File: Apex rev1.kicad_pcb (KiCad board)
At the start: 2 copper layers, 366.4 x 146.1 mm, 230 parts, among them IC1 24SN, IC2 FE1.1S, J1 OLED, J3 USB_A_SMT_FEMALE, J4 USB_A_SMT_FEMALE, P1 Lily58-cache_CONN_01X04, SW1 SW_PUSH, SW2 Rotary_Encoder_Switch, U1 AT90USB1286-MU, X1 12MHz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

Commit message: add ground plane
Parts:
- removed R7: Ferrite 2A, hub_keyboard:R0805
- P1: value Lily58-cache_CONN_01X04 -> Unified C JST
- moved C11 40.8 mm to (337.3, 77.8), turned to 0 degrees
- moved C18 40.0 mm to (319.4, 86.0)
- moved C14 39.8 mm to (331.8, 77.8), turned to 90 degrees
- moved P1 39.3 mm to (334.6, 64.5)
- moved C13 39.1 mm to (319.7, 72.8)
- moved C15 39.1 mm to (333.4, 81.5)
- moved C16 39.1 mm to (319.7, 74.7)
- moved IC2 39.1 mm to (327.2, 77.0)
- moved R17 39.1 mm to (320.2, 70.9)
- moved R18 39.1 mm to (333.6, 74.9)
- moved R8 39.1 mm to (333.6, 73.4)
- moved R9 39.1 mm to (327.4, 69.6)
- moved X1 39.1 mm to (319.4, 82.1)
- moved C17 39.1 mm to (319.4, 79.0)
- moved C22 39.1 mm to (336.9, 80.1)
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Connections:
- net Net-(IC2-Pad15) renamed /USB Hub/DP-
- net Net-(IC2-Pad16) renamed /USB Hub/DP+
- C12 pad +: Net-(C12-Pad+) -> VCC
- C20 pad +: Net-(C12-Pad+) -> VCC
- D1 pad 4: Net-(C12-Pad+) -> VCC
- D2 pad 4: Net-(C12-Pad+) -> VCC
- J3 pad VBUS: Net-(C12-Pad+) -> VCC
- J4 pad VBUS: Net-(C12-Pad+) -> VCC
- R22 pad 2: Net-(C12-Pad+) -> VCC
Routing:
- net VCC: track 63.8 -> 87.6 mm
- net GND: track 41.3 -> 63.1 mm, vias 0 -> 2
- net /USB Hub/DP+: track 0.00 -> 7.25 mm
- net /USB Hub/DP-: track 0.00 -> 6.06 mm
- net Net-(C18-Pad1): track 17.1 -> 12.3 mm
- net /USB Hub/3V3_HUB: track 34.1 -> 33.1 mm
- added copper zone on B.Cu, net GND
- added copper zone on F.Cu, net GND

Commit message: hub controller placement
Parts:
- moved C4 36.3 mm to (466.6, 127.0)
- moved C5 36.3 mm to (462.0, 128.7)
- moved C6 36.3 mm to (457.3, 119.4)
- moved C3 36.3 mm to (453.8, 119.6)
- moved C8 36.3 mm to (458.4, 113.2)
- moved U1 36.3 mm to (465.3, 118.8)
- moved Y1 36.3 mm to (464.5, 109.4)
- moved C1 36.3 mm to (468.7, 109.5)
- moved C2 36.3 mm to (459.7, 109.5)
- moved R4 36.3 mm to (474.8, 120.1)
- moved C11 21.6 mm to (337.1, 99.4)
- moved C14 21.6 mm to (331.5, 99.4)
- moved C17 21.6 mm to (319.2, 100.6)
- moved C22 21.6 mm to (336.6, 101.7)
- moved C9 21.6 mm to (327.0, 89.0)
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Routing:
- net VCC: track 87.6 -> 117.6 mm
- net GND: track 63.1 -> 89.1 mm, vias 2 -> 4
- net Net-(C21-Pad2): track 0.00 -> 19.6 mm
- net /USB Hub/DP+: track 7.25 -> 25.6 mm
- net /USB Hub/DP-: track 6.06 -> 24.3 mm

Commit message: refine sub hub
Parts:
- P1: value Unified C JST -> Lily58-cache_CONN_01X04
- moved D15 5.02 mm to (296.9, 95.9)
- moved D2 3.24 mm to (156.1, 85.2)
- moved C12 0.93 mm to (61.8, 81.4)
- moved D1 0.41 mm to (65.6, 83.6)
- moved R21 0.08 mm to (157.2, 79.0)
- moved R20 0.08 mm to (155.1, 79.0)
- moved R15 0.06 mm to (66.6, 78.9)
- moved R14 0.06 mm to (64.6, 78.9)
- turned R13 to 270 degrees
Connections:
- net Net-(D1-Pad2) renamed /USB Hub/D1-
- net Net-(D1-Pad3) renamed /USB Hub/D1+
- net Net-(D2-Pad2) renamed /USB Hub/D2-
- net Net-(D2-Pad3) renamed /USB Hub/D2+
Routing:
- net VCC: track 117.6 -> 439.3 mm
- net /USB Hub/D1-: track 0.00 -> 280.4 mm, vias 0 -> 2
- net /USB Hub/D1+: track 0.00 -> 279.2 mm, vias 0 -> 2
- net /USB Hub/D2-: track 0.00 -> 191.5 mm, vias 0 -> 2
- net /USB Hub/D2+: track 0.00 -> 190.2 mm, vias 0 -> 2
- net Net-(C19-Pad2): track 0.00 -> 7.06 mm
- net GND: vias 4 -> 6
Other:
- net class Default: via_dia 0.8 -> 0.6222

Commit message: route keys
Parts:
- moved R4 130.4 mm to (348.2, 151.3), turned to 180 degrees
- moved C1 125.9 mm to (354.3, 161.9), turned to 270 degrees
- moved Y1 118.3 mm to (358.5, 161.9), turned to 0 degrees
- moved U1 112.8 mm to (357.7, 152.5), turned to 180 degrees
- moved C4 111.6 mm to (356.4, 144.3), turned to 0 degrees
- moved C2 109.7 mm to (363.3, 161.9), turned to 90 degrees
- moved R3 104.3 mm to (372.4, 179.3), turned to 270 degrees
- moved C8 104.1 mm to (364.6, 158.2), turned to 270 degrees
- moved C5 102.1 mm to (360.9, 142.7), turned to 180 degrees
- moved SW1 98.7 mm to (378.9, 178.7), turned to 0 degrees
- moved C6 97.1 mm to (365.7, 151.9), turned to 90 degrees
- moved C3 90.6 mm to (369.1, 151.8), turned to 0 degrees
- moved D50 17.1 mm to (314.5, 131.1)
- moved D80 16.5 mm to (59.9, 181.2)
- moved D77 15.6 mm to (267.5, 167.3)
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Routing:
- net ROW0: track 0.00 -> 338.9 mm, vias 0 -> 2
- net ROW5: track 0.00 -> 324.7 mm
- net ROW2: track 0.00 -> 319.3 mm
- net ROW1: track 0.00 -> 318.6 mm
- net ROW4: track 0.00 -> 287.7 mm
- net ROW3: track 0.00 -> 249.3 mm
- net COL15: track 0.00 -> 135.2 mm
- net COL10: track 0.00 -> 134.8 mm
- net COL13: track 0.00 -> 124.7 mm, vias 0 -> 1
- net COL11: track 0.00 -> 124.0 mm
- net VCC: track 439.3 -> 562.7 mm
- net D+: track 0.00 -> 119.9 mm
- net COL2: track 0.00 -> 119.6 mm
- net COL12: track 0.00 -> 118.5 mm
- net D-: track 0.00 -> 118.4 mm
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
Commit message: routed keys
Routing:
- net VCC: track 562.7 -> 606.9 mm
- net SDA: track 2.64 -> 35.9 mm, vias 0 -> 2
- net SCL: track 2.85 -> 35.8 mm, vias 0 -> 2
- net GND: track 94.0 -> 115.5 mm, vias 6 -> 8
- net Net-(D20-Pad2): track 0.00 -> 12.6 mm
- net Net-(D36-Pad2): track 0.00 -> 12.1 mm
- net Net-(D23-Pad2): track 0.00 -> 10.8 mm
- net Net-(D22-Pad2): track 0.00 -> 10.4 mm
- net Net-(D21-Pad2): track 0.00 -> 10.4 mm
- net Net-(D25-Pad2): track 0.00 -> 9.66 mm
- net Net-(D24-Pad2): track 0.00 -> 9.65 mm
- net Net-(D26-Pad2): track 0.00 -> 9.33 mm
- net Net-(D34-Pad2): track 0.00 -> 9.03 mm
- net Net-(D33-Pad2): track 0.00 -> 9.01 mm
- net Net-(D27-Pad2): track 0.00 -> 9.00 mm
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
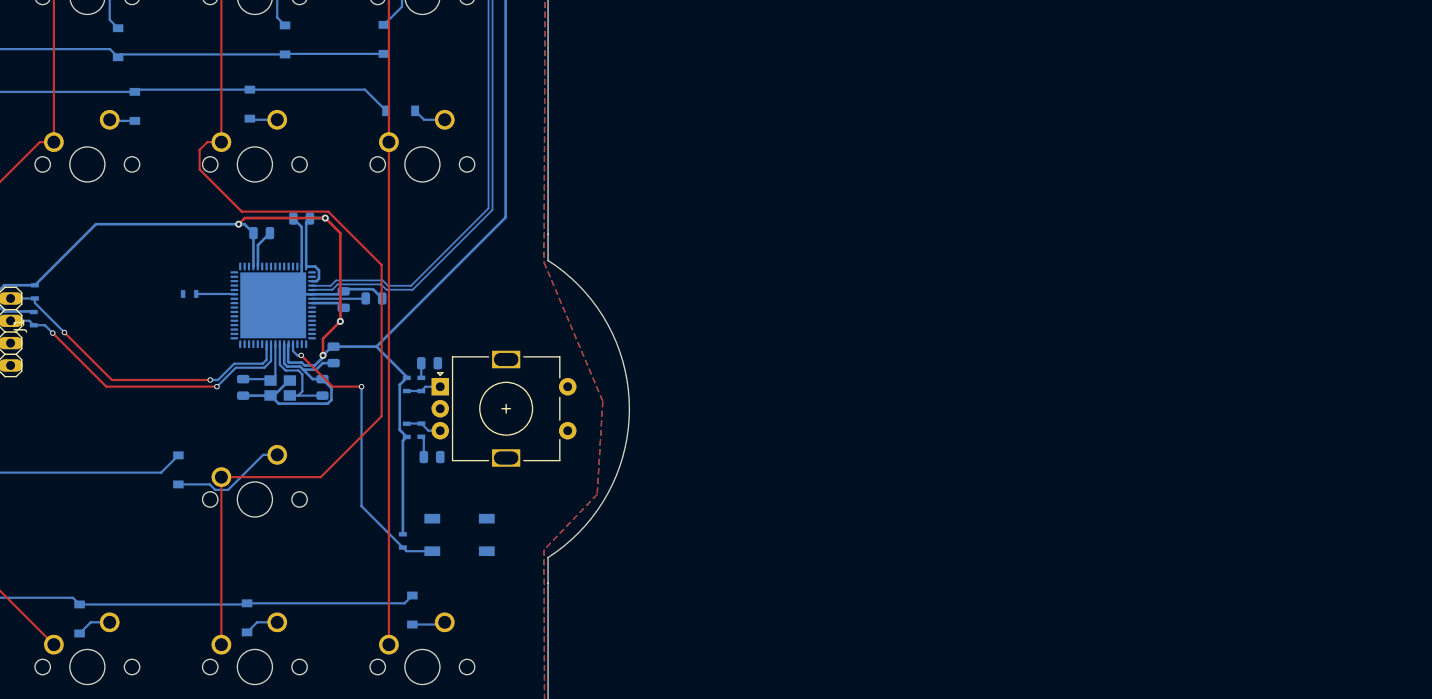
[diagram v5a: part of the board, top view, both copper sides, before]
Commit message: assigned some pins
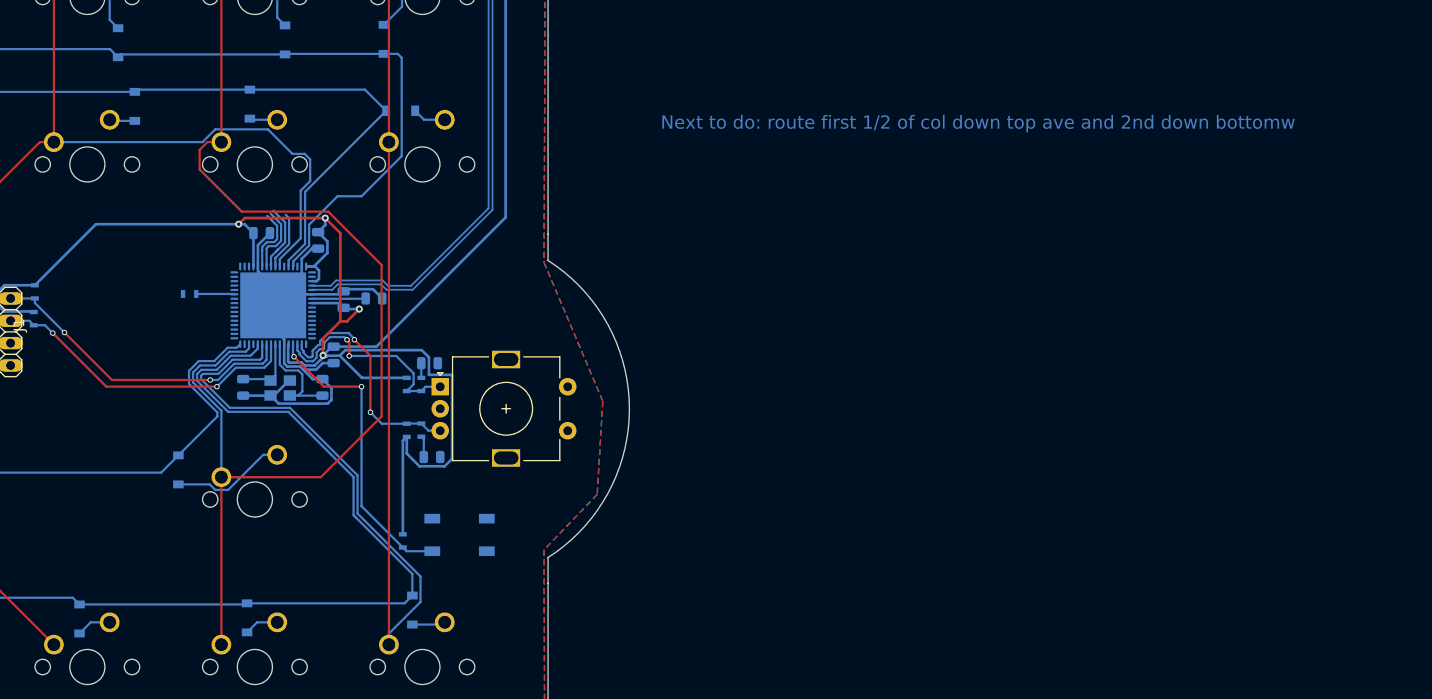
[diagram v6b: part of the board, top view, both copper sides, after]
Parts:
- moved C5 3.10 mm to (362.8, 145.2), turned to 270 degrees
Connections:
- net ENC1 renamed Net-(C25-Pad1)
- net ENC2 renamed Net-(C26-Pad1)
- U1 pad 18: Net-(U1-Pad18) -> ROT2
- U1 pad 19: Net-(U1-Pad19) -> ROT1
- U1 pad 27: Net-(U1-Pad27) -> COL16
- U1 pad 28: Net-(U1-Pad28) -> ROW5
- U1 pad 30: Net-(U1-Pad30) -> COL15
- U1 pad 32: Net-(U1-Pad32) -> ROW4
- U1 pad 58: Net-(U1-Pad58) -> COL14
- U1 pad 60: Net-(U1-Pad60) -> ROW2
- U1 pad 61: Net-(U1-Pad61) -> ROW1
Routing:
- net COL16: track 104.8 -> 161.8 mm
- net ROW5: track 324.7 -> 372.7 mm
- net COL14: track 114.1 -> 158.9 mm
- net VCC: track 606.9 -> 641.5 mm
- net ROW1: track 318.6 -> 351.8 mm
- net ROT2: track 4.15 -> 27.0 mm, vias 0 -> 2
- net ROW2: track 319.3 -> 341.6 mm
- net ROT1: track 4.01 -> 25.4 mm, vias 0 -> 2
- net COL15: track 135.2 -> 156.5 mm
- net ROW4: track 287.7 -> 307.6 mm
- net Net-(U1-Pad56): track 0.00 -> 8.12 mm
- net Net-(U1-Pad55): track 0.00 -> 7.69 mm
- net Net-(U1-Pad54): track 0.00 -> 7.43 mm
- net GND: track 115.5 -> 122.6 mm
- net Net-(U1-Pad57): track 0.00 -> 6.71 mm
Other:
- board text added: "Next to do: route first 1/2 of col down top ave and 2nd down bottomw"

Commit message: completed routing matrix
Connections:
- U1 pad 15: Net-(U1-Pad15) -> ROT2
- U1 pad 16: Net-(U1-Pad16) -> ROT1
- U1 pad 18: ROT2 -> Net-(U1-Pad18)
- U1 pad 19: ROT1 -> Net-(U1-Pad19)
- U1 pad 33: Net-(U1-Pad33) -> ROW3
- U1 pad 34: Net-(U1-Pad34) -> COL13
- U1 pad 35: Net-(U1-Pad35) -> COL11
- U1 pad 36: Net-(U1-Pad36) -> COL10
- U1 pad 37: Net-(U1-Pad37) -> COL9
- U1 pad 38: Net-(U1-Pad38) -> COL8
- U1 pad 39: Net-(U1-Pad39) -> COL7
- U1 pad 40: Net-(U1-Pad40) -> COL6
- U1 pad 41: Net-(U1-Pad41) -> COL0
- U1 pad 42: Net-(U1-Pad42) -> COL1
- U1 pad 50: Net-(U1-Pad50) -> COL2
- U1 pad 51: Net-(U1-Pad51) -> COL3
- U1 pad 54: Net-(U1-Pad54) -> COL4
- U1 pad 55: Net-(U1-Pad55) -> COL5
- U1 pad 56: Net-(U1-Pad56) -> COL12
- U1 pad 57: Net-(U1-Pad57) -> ROW0
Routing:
- net COL0: track 114.6 -> 446.3 mm
- net COL1: track 93.4 -> 401.8 mm
- net COL2: track 119.6 -> 392.1 mm
- net COL3: track 95.6 -> 349.7 mm
- net COL4: track 95.6 -> 336.8 mm
- net COL5: track 116.8 -> 339.5 mm
- net COL6: track 99.5 -> 305.1 mm
- net COL7: track 99.5 -> 285.9 mm
- net COL8: track 99.5 -> 266.6 mm
- net COL9: track 100.5 -> 248.3 mm
- net COL10: track 134.8 -> 263.8 mm
- net COL11: track 124.0 -> 233.5 mm
- net ROW0: track 338.9 -> 436.1 mm, vias 2 -> 4
- net COL12: track 118.5 -> 208.1 mm
- net COL13: track 124.7 -> 195.6 mm
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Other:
- board text removed: "Next to do: route first 1/2 of col down top ave and 2nd down bottomw"

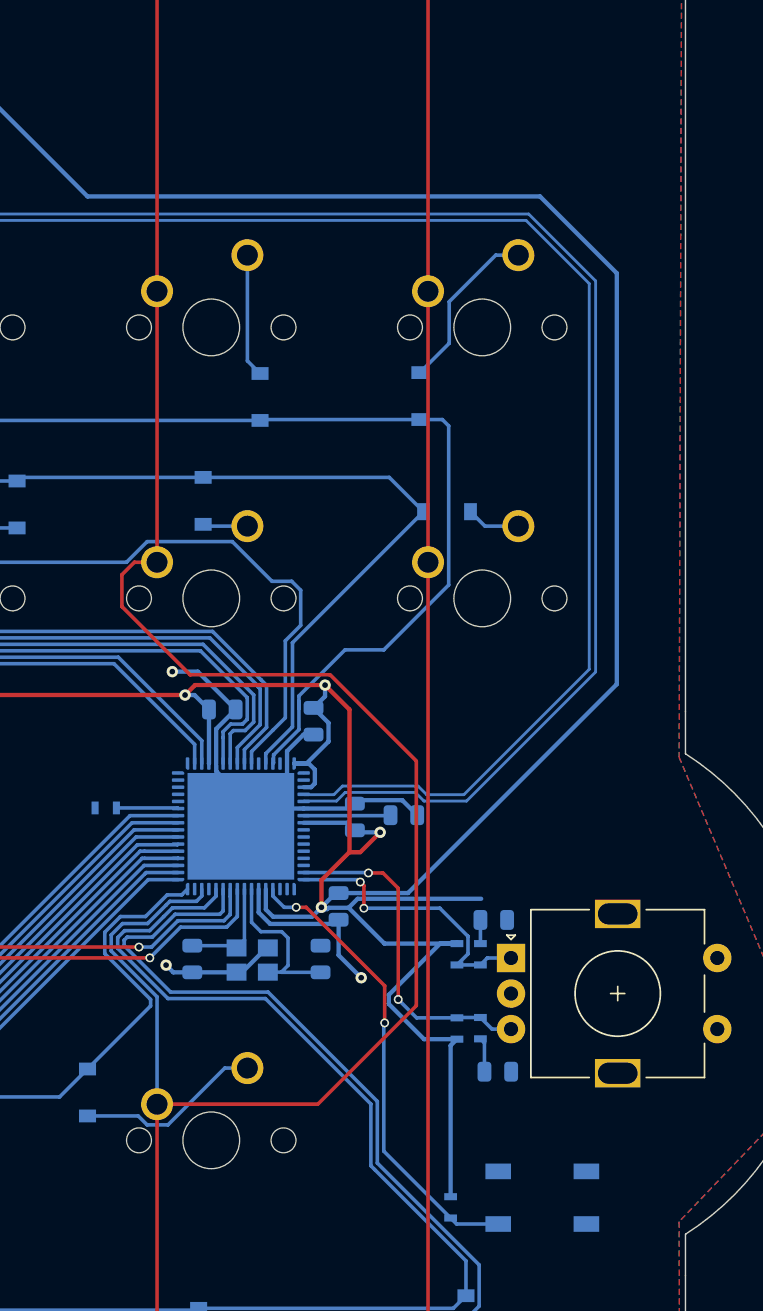
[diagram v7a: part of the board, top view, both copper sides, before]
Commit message: Add ISP header
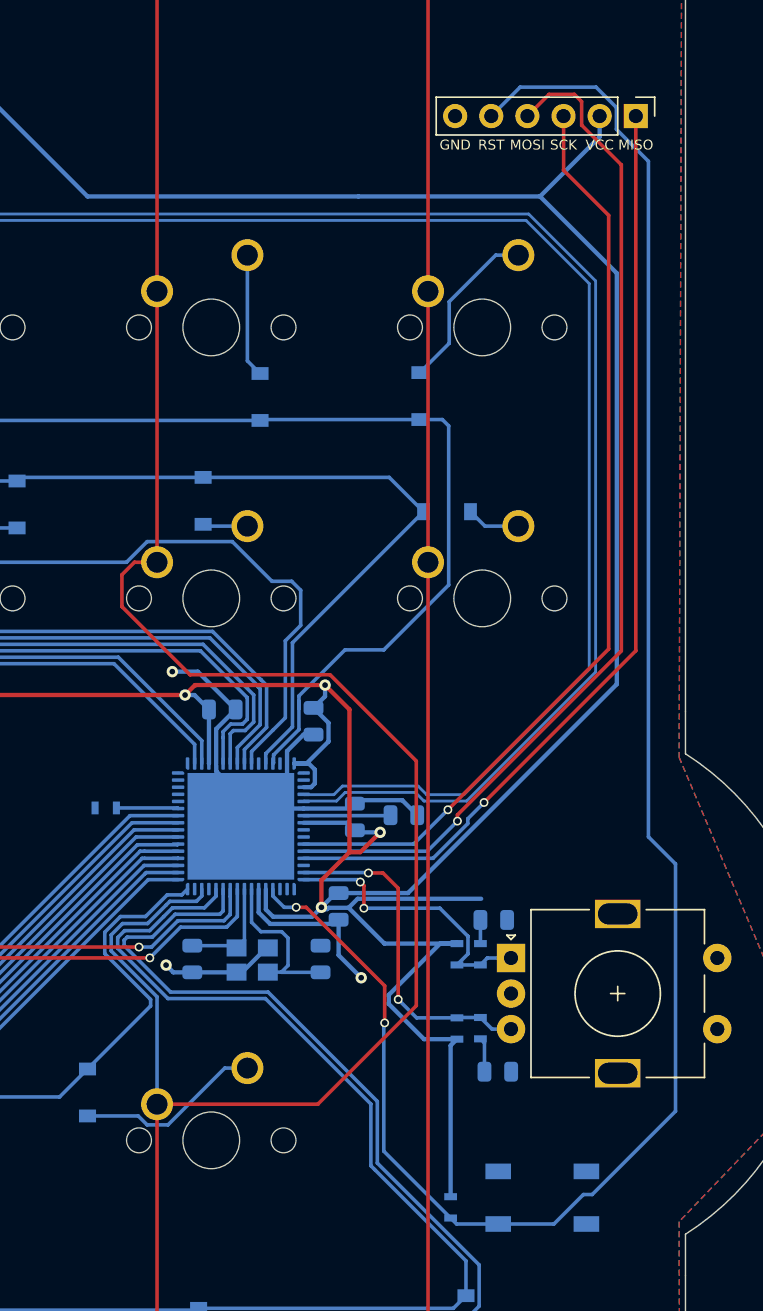
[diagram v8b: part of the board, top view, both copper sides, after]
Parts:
- added J2: AVR-ISP-6, 1_Keyboard Footprints:ICSP-Header, F.Cu at (385.4, 102.6)
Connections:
- net Net-(R3-Pad2) renamed RST
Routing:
- net RST: track 32.8 -> 131.0 mm
- net MOSI: track 0.00 -> 72.9 mm, vias 0 -> 1
- net MISO: track 0.00 -> 67.2 mm, vias 0 -> 1
- net SCLK: track 0.00 -> 65.9 mm, vias 0 -> 1
- net VCC: track 630.3 -> 637.7 mm
